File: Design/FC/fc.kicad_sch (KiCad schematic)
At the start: 1 part, among them U1 STM32H747BIT6

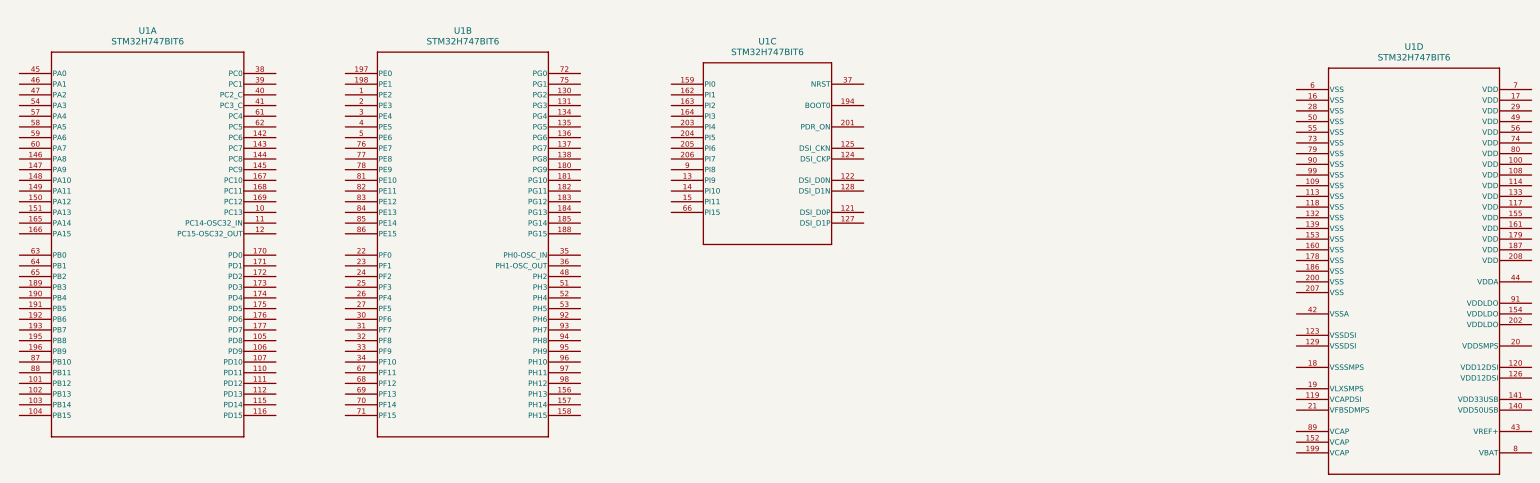
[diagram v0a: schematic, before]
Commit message: finished power layout for fc
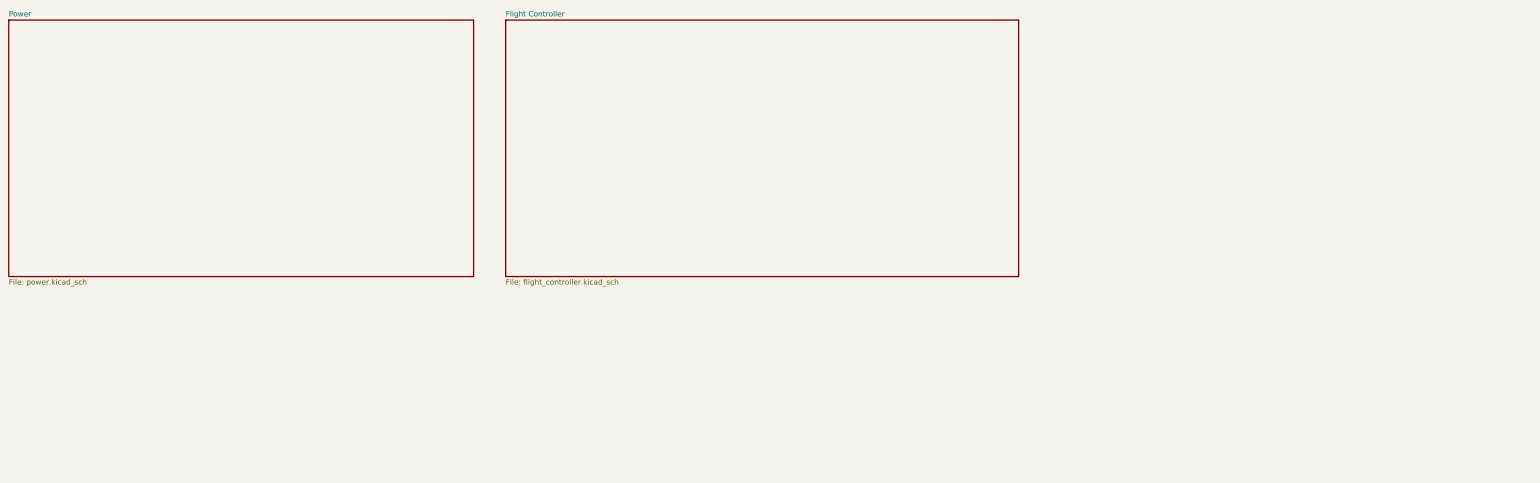
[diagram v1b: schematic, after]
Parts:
- removed U1: STM32H747BIT6, Lib:STM32H747BIT6-LQFP-208, symbol STM32H747BIT6-LQFP208:STM32H747BIT6
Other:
- added sheet Flight Controller (flight_controller.kicad_sch)
- added sheet Power (power.kicad_sch)
